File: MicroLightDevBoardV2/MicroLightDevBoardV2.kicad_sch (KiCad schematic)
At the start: 83 parts, among them J1 Conn_01x02_Socket, J10 Conn_01x02_Socket, J11 Conn_01x02_Socket, J12 TYPE-C-31-M-12, J13 Conn_01x02_Socket, J14 Conn_01x02_Socket, J15 Conn_01x02_Socket, J16 Conn_01x04_Socket, J17 Conn_01x02_Socket, J18 Conn_01x02_Socket, J19 Conn_01x04_Socket, J2 Conn_01x02_Socket, J20 Conn_01x04_Socket, J21 Conn_01x02_Socket, J22 Conn_01x02_Socket, J23 Conn_01x02_Socket, J24 Conn_01x02_Socket, J25 Conn_01x02_Socket, J26 Conn_01x04_Socket, J27 Conn_01x02_Socket, J28 Conn_01x04_Socket, J29 Conn_01x04_Socket, J3 Conn_01x04_Socket, J30 Conn_01x04_Socket, J31 Conn_01x04_Socket, J32 Conn_01x04_Socket, J33 Conn_01x04_Socket, J34 Conn_01x04_Socket, J35 Conn_01x04_Socket, J36 Conn_01x04_Socket, J37 Conn_01x04_Socket, J38 Conn_01x04_Socket, J39 Conn_01x04_Socket, J4 Conn_01x04_Socket, J40 Conn_01x04_Socket, J41 Conn_01x04_Socket, J42 Conn_01x04_Socket, J43 Conn_01x04_Socket, J44 Conn_01x04_Socket, J45 Conn_01x04_Socket, J46 Conn_01x04_Socket, J47 Conn_01x04_Socket, J48 Conn_01x04_Socket, J49 Conn_01x04_Socket, J5 Conn_01x05_Socket, J50 Conn_01x04_Socket, J6 Conn_01x05_Socket, J7 Conn_01x05_Socket, J8 Conn_01x05_Socket, J9 Conn_01x02_Socket, U1 BQ25180, U2 ATtiny3226-M, U3 S-85S1AB33-I6T1U, U4 B3U-1000P, U5 B3U-1000P, U6 USBLC6-2P6, U7 MC3479

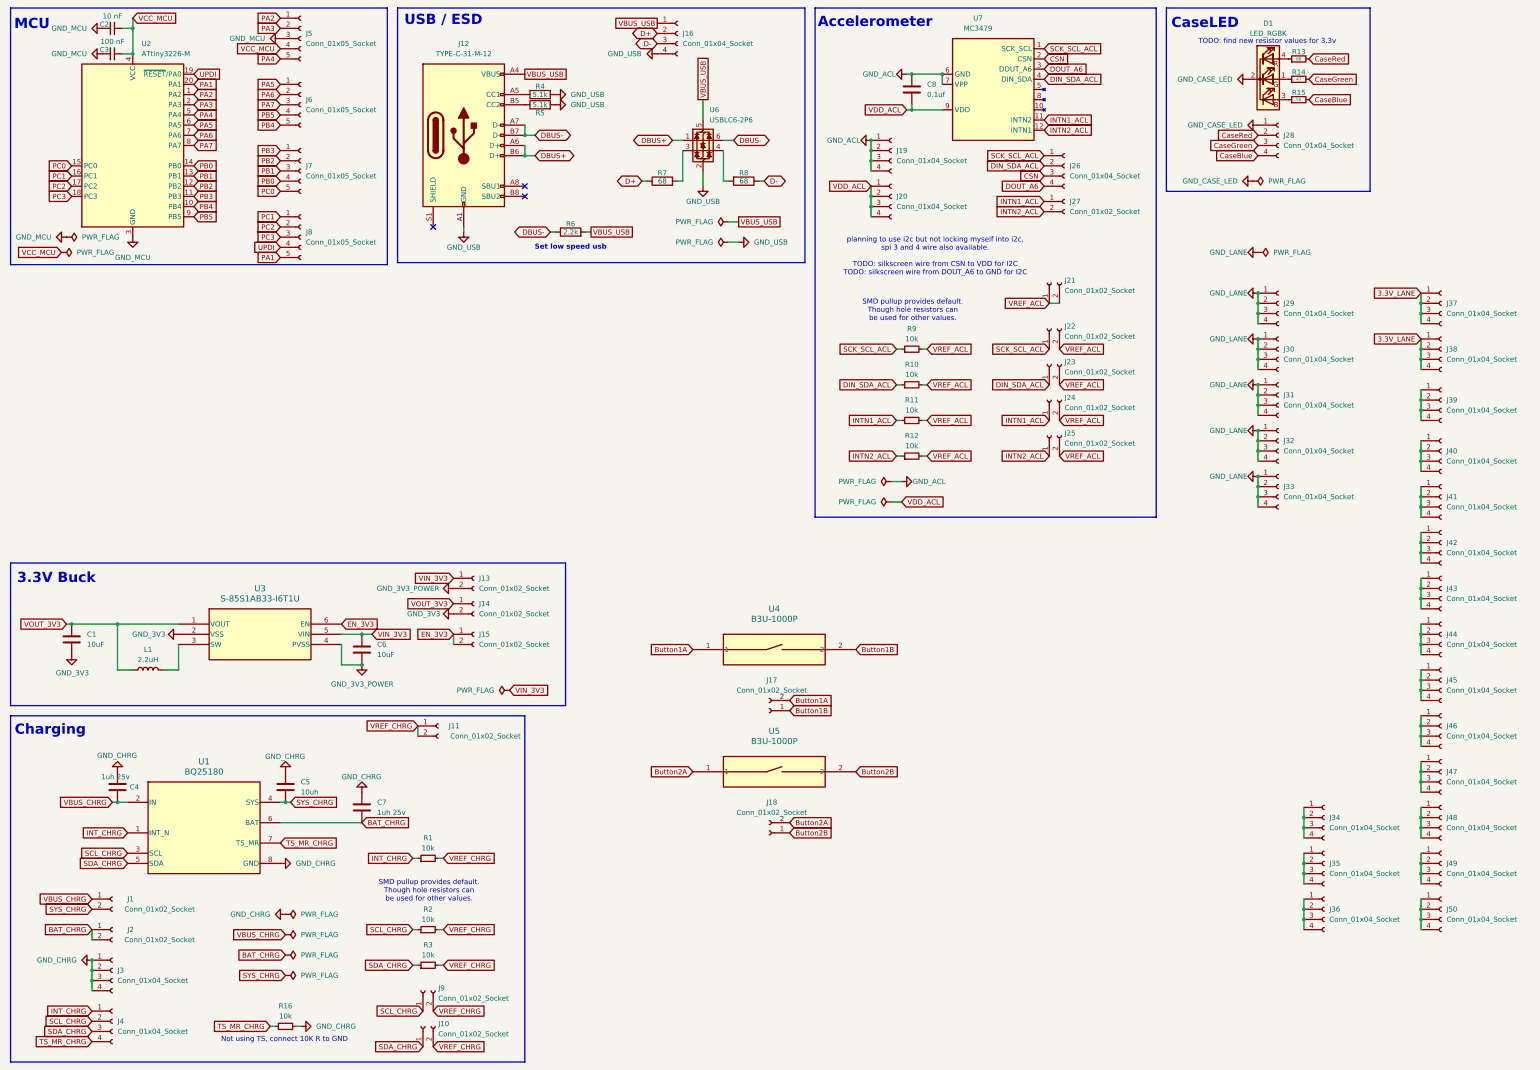
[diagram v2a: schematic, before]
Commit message: add lcsc part numbers
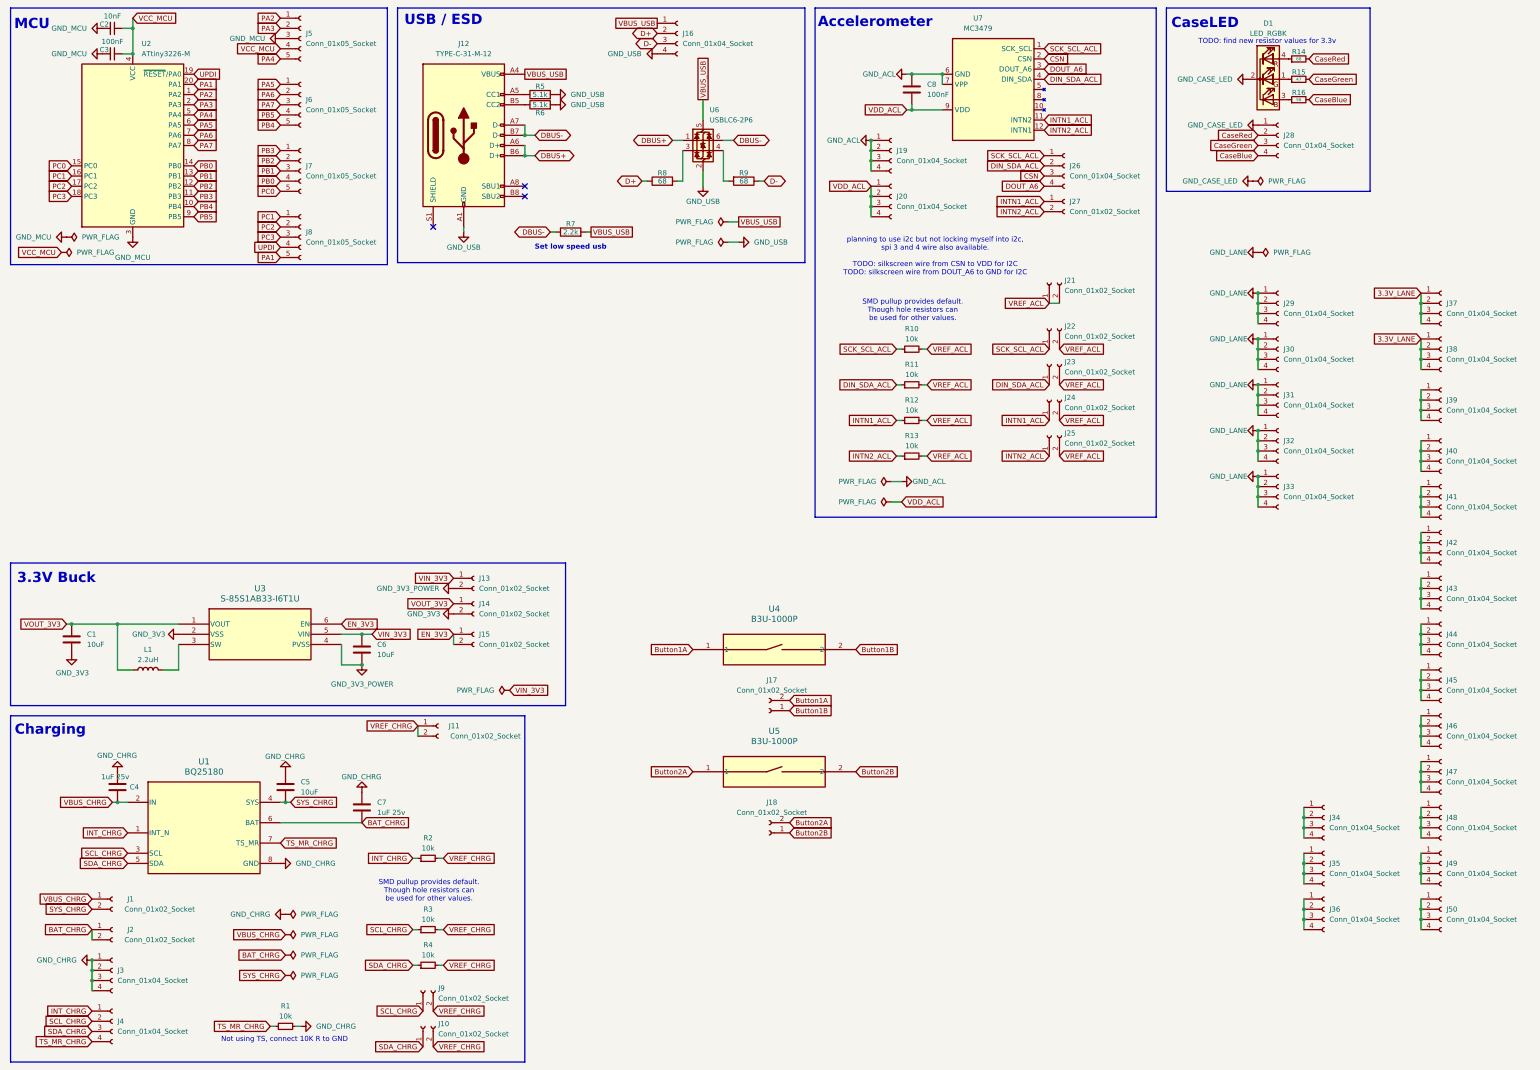
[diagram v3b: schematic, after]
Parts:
- C2: value 10 nF -> 10nF
- C3: value 100 nF -> 100nF
- C4, C7: value 1uh 25v -> 1uF 25v
- C5: value 10uh -> 10uF
- C8: value 0.1uf -> 100nF
- renumbered R16 to R1, R9 to R10, R10 to R11, R11 to R12, R12 to R13, R13 to R14, R14 to R15, R15 to R16, R1 to R2, R2 to R3, R3 to R4, R4 to R5, R5 to R6, R6 to R7, R7 to R8, R8 to R9

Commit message: exported lcsc ids to schematic symbols
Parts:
- C1, C5, C6: LCSC (none) -> C96446
- C2: LCSC (none) -> C57112
- C3, C8: LCSC (none) -> C14663
- C4, C7: LCSC (none) -> C15849
- D1: LCSC (none) -> C2874181
- J1, J10, J11, J13, J14, J15, J17, J18, J2, J21, J22, J23, J24, J25, J27, J9: LCSC (none) -> C49661
- J12: LCSC (none) -> C165948
- J16, J19, J20, J26, J28, J29, J3, J30, J31, J32, J33, J34, J35, J36, J37, J38, J39, J4, J40, J41, J42, J43, J44, J45, J46, J47, J48, J49, J50: LCSC (none) -> C2718488
- J5, J6, J7, J8: LCSC (none) -> C50950
- R1, R10, R11, R12, R13, R2, R3, R4: LCSC (none) -> C25804
- R14, R16, R8, R9: LCSC (none) -> C27592
- R15: LCSC (none) -> C23182
- R5, R6: LCSC (none) -> C23186
- R7: LCSC (none) -> C4190
- U1: LCSC (none) -> C3682423
- U4, U5: LCSC (none) -> C231329
- U6: LCSC (none) -> C15999

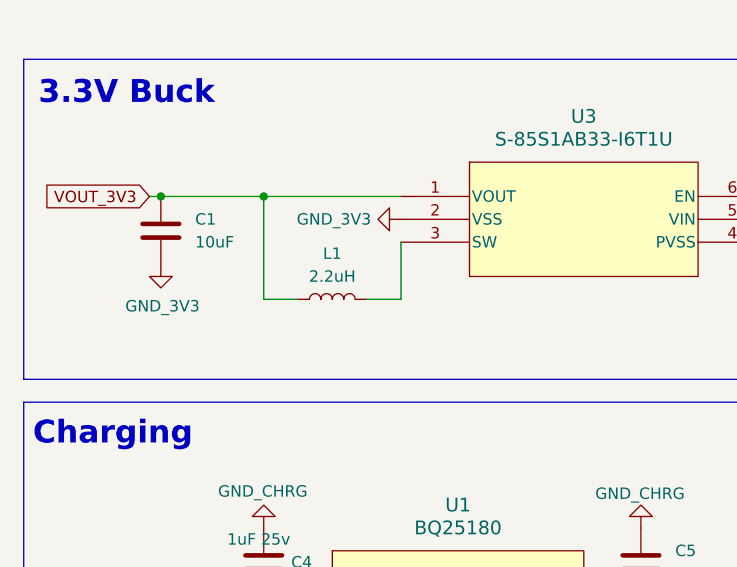
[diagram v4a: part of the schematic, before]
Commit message: changed inductor so jlcpcb doesn't try to autofill some random one
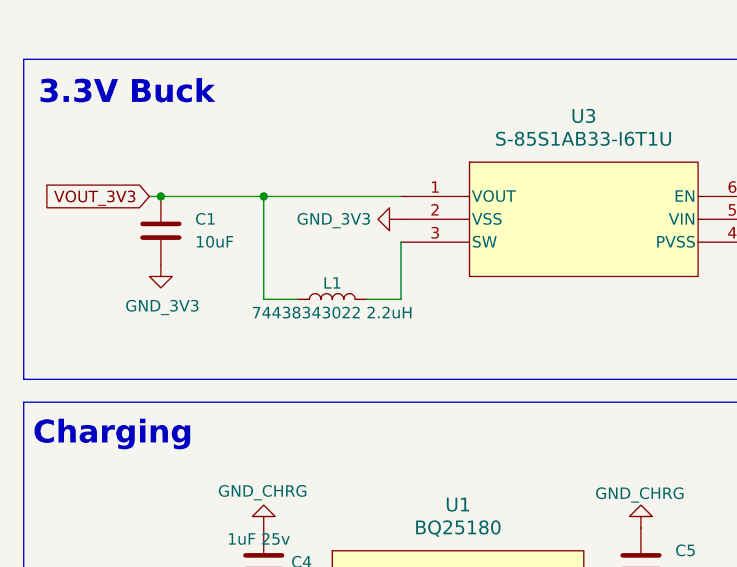
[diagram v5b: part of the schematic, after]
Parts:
- L1: value 2.2uH -> 74438343022 2.2uH
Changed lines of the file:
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@@
 		(on_board yes)
 		(dnp no)
-		(fields_autoplaced yes)
 		(property "Reference" "L1"
-			(at 49.53 175.26 90)
+			(at 49.53 178.562 90)
 			(effects
 				(font
@@
 			)
 		)
-		(property "Value" "2.2uH"
-			(at 49.53 177.8 90)
+		(property "Value" "74438343022 2.2uH"
+			(at 49.53 181.864 90)
 			(effects
 				(font

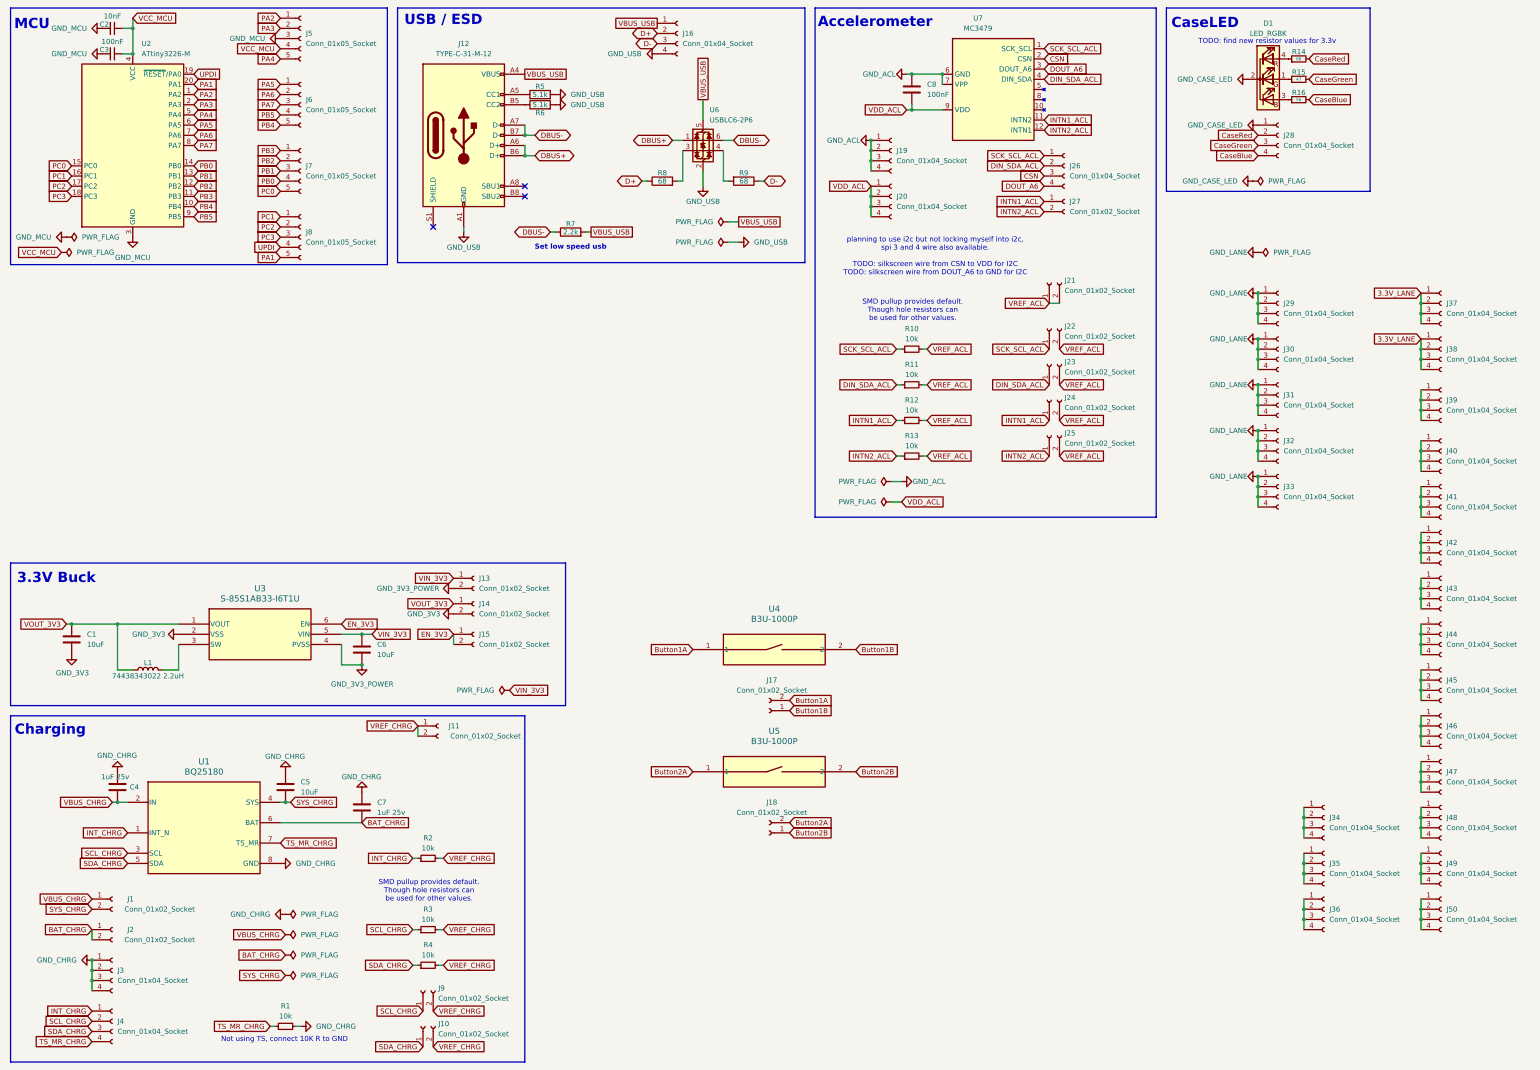
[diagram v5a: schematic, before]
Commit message: updated led resistor values for 3.3v
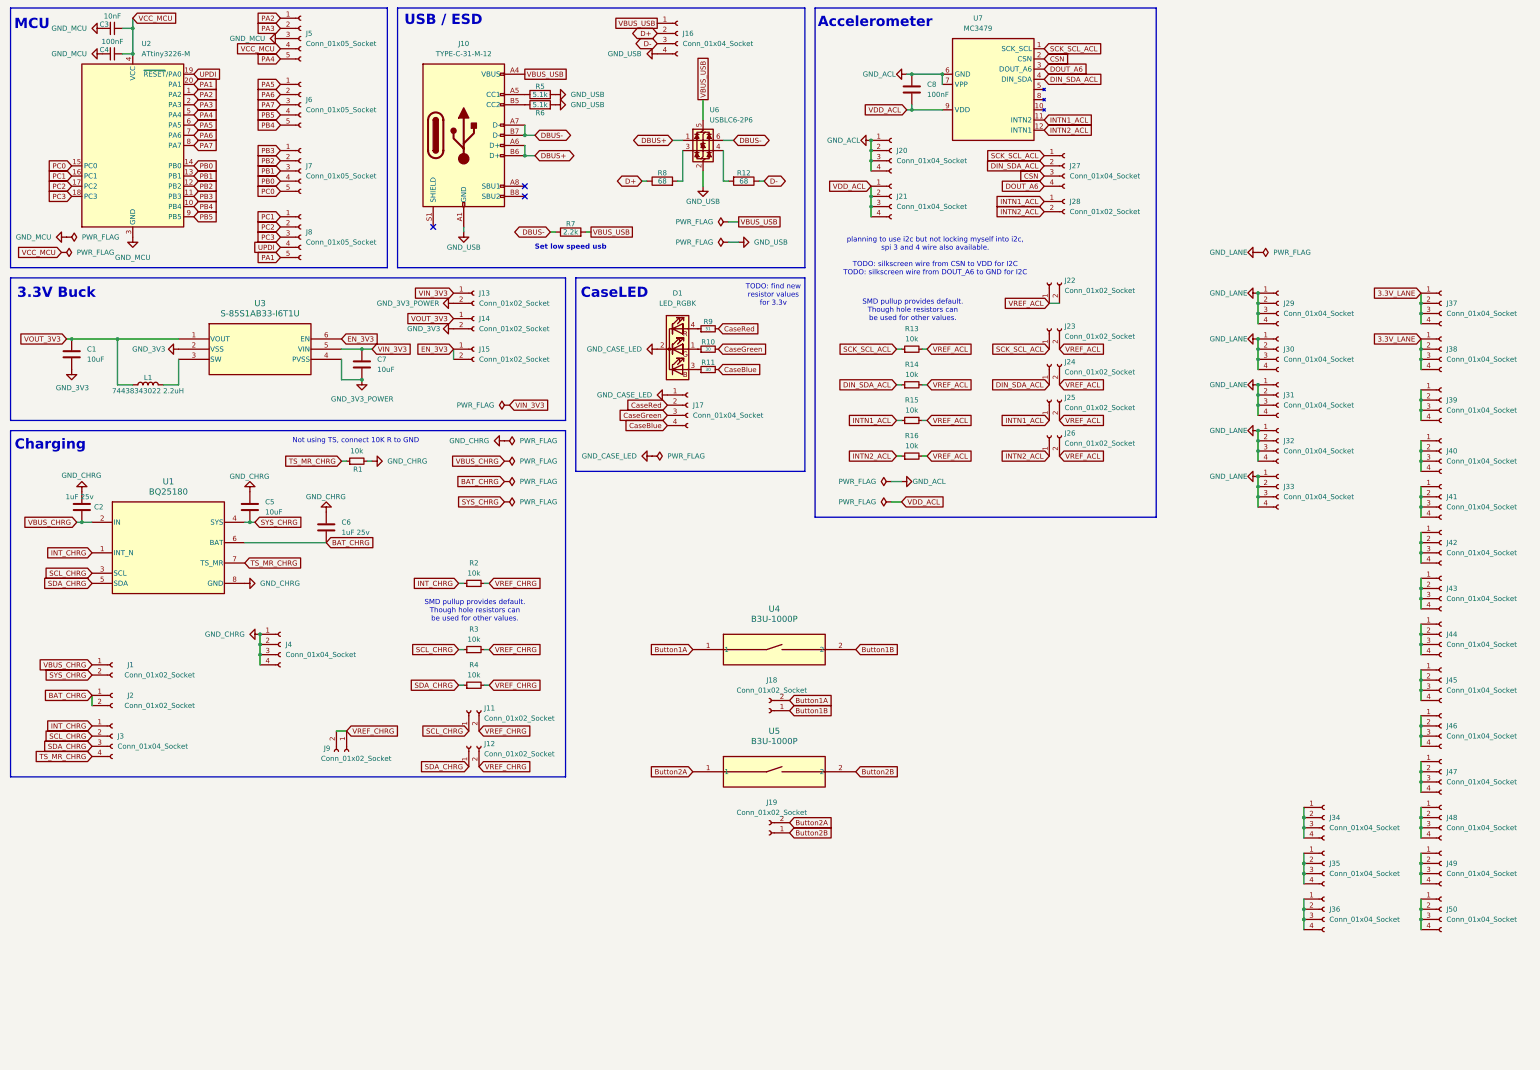
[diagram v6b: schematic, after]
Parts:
- C2: renamed from C4; LCSC C15849 -> C14663
- C3: renamed from C2; LCSC C57112 -> C15849
- C4: renamed from C3; LCSC C14663 -> C57112
- C6: renamed from C7; LCSC C15849 -> C96446
- C7: renamed from C6; LCSC C96446 -> C15849
- J10: renamed from J12; LCSC C165948 -> C49661
- J12: renamed from J10; LCSC C49661 -> C165948
- J17: renamed from J28; LCSC C2718488 -> C49661
- J18: renamed from J17; LCSC C49661 -> C2718488
- J20: renamed from J19; LCSC C2718488 -> C49661
- J22: renamed from J21; LCSC C49661 -> C2718488
- J27: renamed from J26; LCSC C2718488 -> C49661
- J28: renamed from J27; LCSC C49661 -> C2718488
- R10: renamed from R15; value 47 -> 30; LCSC C23182 -> C23140
- R11: renamed from R16; value 56 -> 30; LCSC C27592 -> C23140
- R13: renamed from R10; LCSC C25804 -> C23140
- R14: renamed from R11; LCSC C25804 -> C23140
- R15: renamed from R12; LCSC C25804 -> C27592
- R9: renamed from R14; value 68 -> 51; LCSC C27592 -> C23197
- renumbered J9 to J11, J18 to J19, J20 to J21, J22 to J23, J23 to J24, J24 to J25, J25 to J26, J4 to J3, J3 to J4, J11 to J9, R9 to R12, R13 to R16
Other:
- moved on the sheet: C1, C2, C5, C6, C7, D1, J1, J11, J12, J13, J14, J15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

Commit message: correct part numbers and generated ordering files
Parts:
- C2: LCSC C14663 -> C15849
- C3: LCSC C15849 -> C57112
- C4: LCSC C57112 -> C14663
- C6: LCSC C96446 -> C15849
- C7: LCSC C15849 -> C96446
- J10: LCSC C49661 -> C165948
- J12: LCSC C165948 -> C49661
- J17, J20, J27: LCSC C49661 -> C2718488
- J18, J22, J28: LCSC C2718488 -> C49661
- R13, R14: LCSC C23140 -> C25804
- R15: LCSC C27592 -> C25804
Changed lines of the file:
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@@
 			)
 		)
-		(property "LCSC" "C14663"
+		(property "LCSC" "C15849"
 			(at 36.068 139.7 0)
 			(effects
@@
 			)
 		)
-		(property "LCSC" "C23140"
+		(property "LCSC" "C25804"
 			(at 240.03 95.25 0)
 			(effects
@@
 			)
 		)
-		(property "LCSC" "C15849"
+		(property "LCSC" "C96446"
 			(at 106.68 102.8699 0)
 			(effects
@@
 			)
 		)
-		(property "LCSC" "C27592"
+		(property "LCSC" "C25804"
 			(at 240.03 113.03 0)
 			(effects
@@
 			)
 		)
-		(property "LCSC" "C57112"
+		(property "LCSC" "C14663"
 			(at 38.608 25.654 0)
 			(effects
@@
 			)
 		)
-		(property "LCSC" "C49661"
+		(property "LCSC" "C165948"
 			(at 128.27 24.13 0)
 			(effects
@@
 			)
 		)
-		(property "LCSC" "C2718488"
+		(property "LCSC" "C49661"
 			(at 278.13 83.1849 0)
 			(effects
@@
 			)
 		)
-		(property "LCSC" "C2718488"
+		(property "LCSC" "C49661"
 			(at 205.105 182.88 0)
 			(effects
@@
 			)
 		)
-		(property "LCSC" "C23140"
+		(property "LCSC" "C25804"
 			(at 240.03 104.14 0)
 			(effects
@@
 			)
 		)
-		(property "LCSC" "C49661"
+		(property "LCSC" "C2718488"
 			(at 236.22 50.7999 0)
 			(effects
@@
 			)
 		)
-		(property "LCSC" "C96446"
+		(property "LCSC" "C15849"
 			(at 97.79 143.5099 0)
 			(effects
@@
 			)
 		)
-		(property "LCSC" "C15849"
+		(property "LCSC" "C57112"
 			(at 38.608 19.304 0)
 			(effects
@@
 			)
 		)
-		(property "LCSC" "C49661"
+		(property "LCSC" "C2718488"
 			(at 185.42 114.2999 0)
 			(effects
@@
 			)
 		)
-		(property "LCSC" "C165948"
+		(property "LCSC" "C49661"
 			(at 133.35 198.7549 0)
 			(effects
@@
 			)
 		)
-		(property "LCSC" "C49661"
+		(property "LCSC" "C2718488"
 			(at 279.4 54.6099 0)
 			(effects
@@
 			)
 		)
-		(property "LCSC" "C2718488"
+		(property "LCSC" "C49661"
 			(at 279.4 63.4999 0)
 			(effects
